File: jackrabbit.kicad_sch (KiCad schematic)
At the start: 62 parts, among them J1 USB_C, J2 PinHeader_2.54mm_02x10, J3 PinHeader_2.54mm_02x04, J4 PinHeader_2.54mm_02x04, J5 PinHeader_2.54mm_01x04, J6 PinHeader_2.54mm_01x03, SW1 SW_Push, SW2 SW_Push, U1 MIC5319-3.3YD5, U2 74LVX245, U3 W25Q16JVSNIQ, U4 RP2040, U5 74LVX245, Y1 ECS-120-18-33-JGN

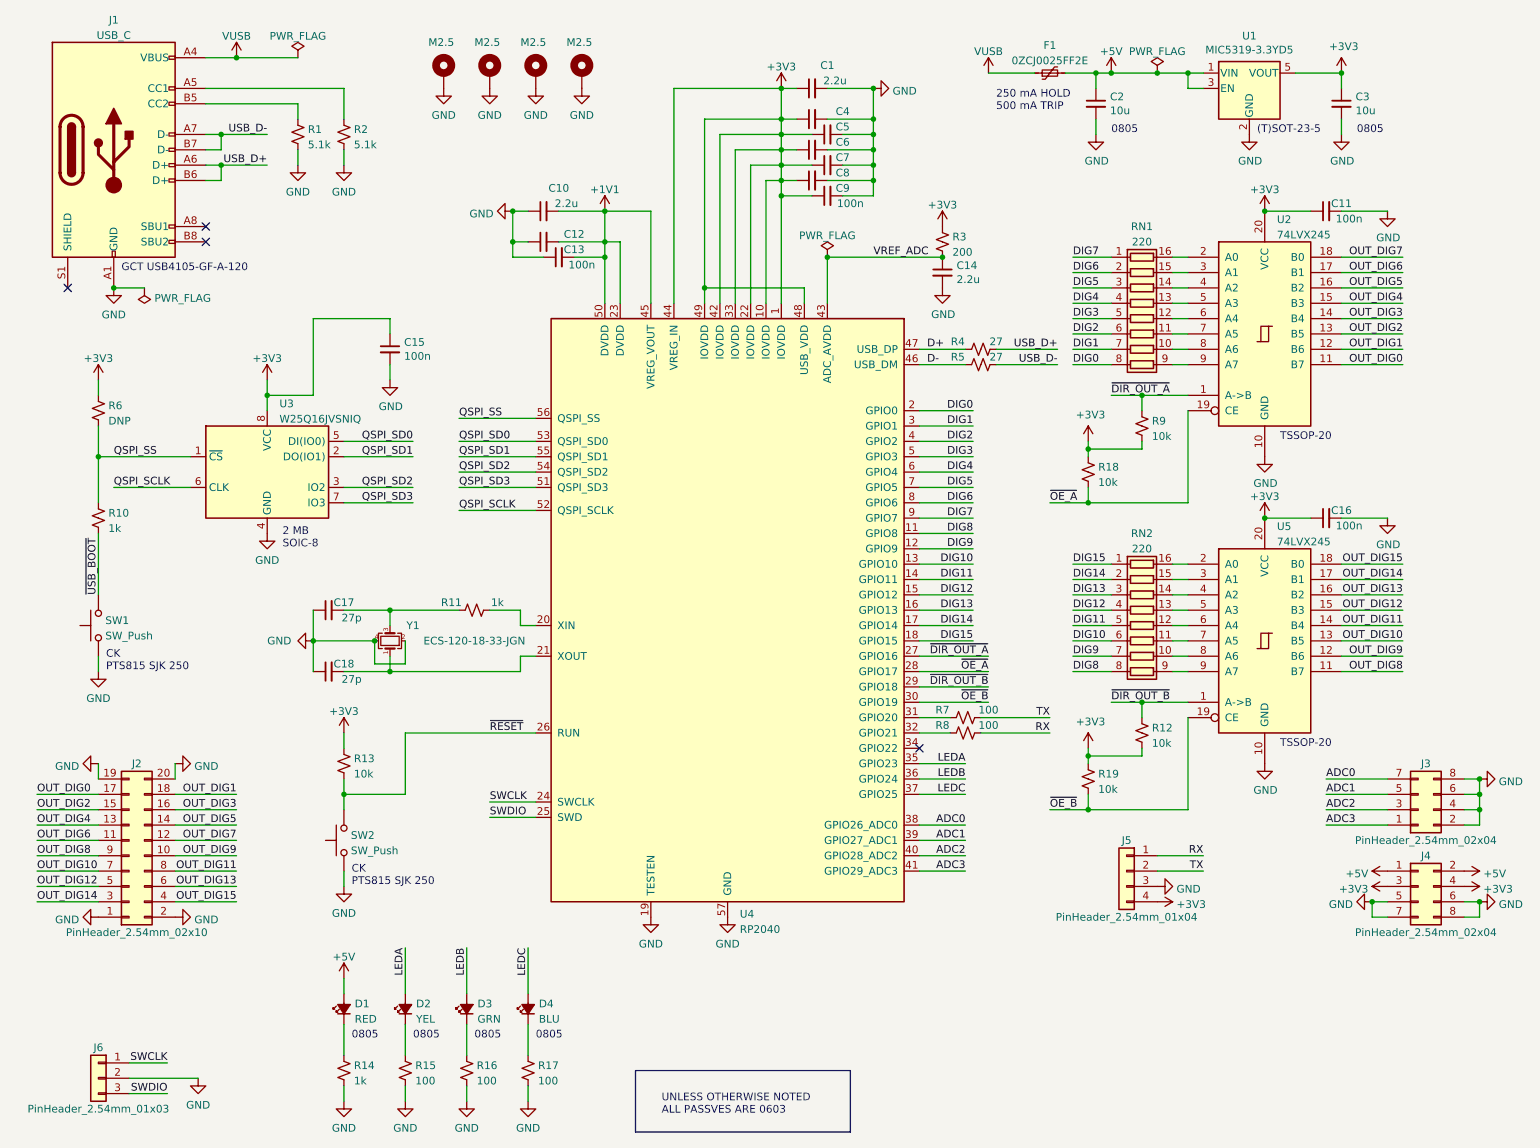
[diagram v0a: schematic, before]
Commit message: Connect bootsel button to a GPIO; remove connectors for which we have no room
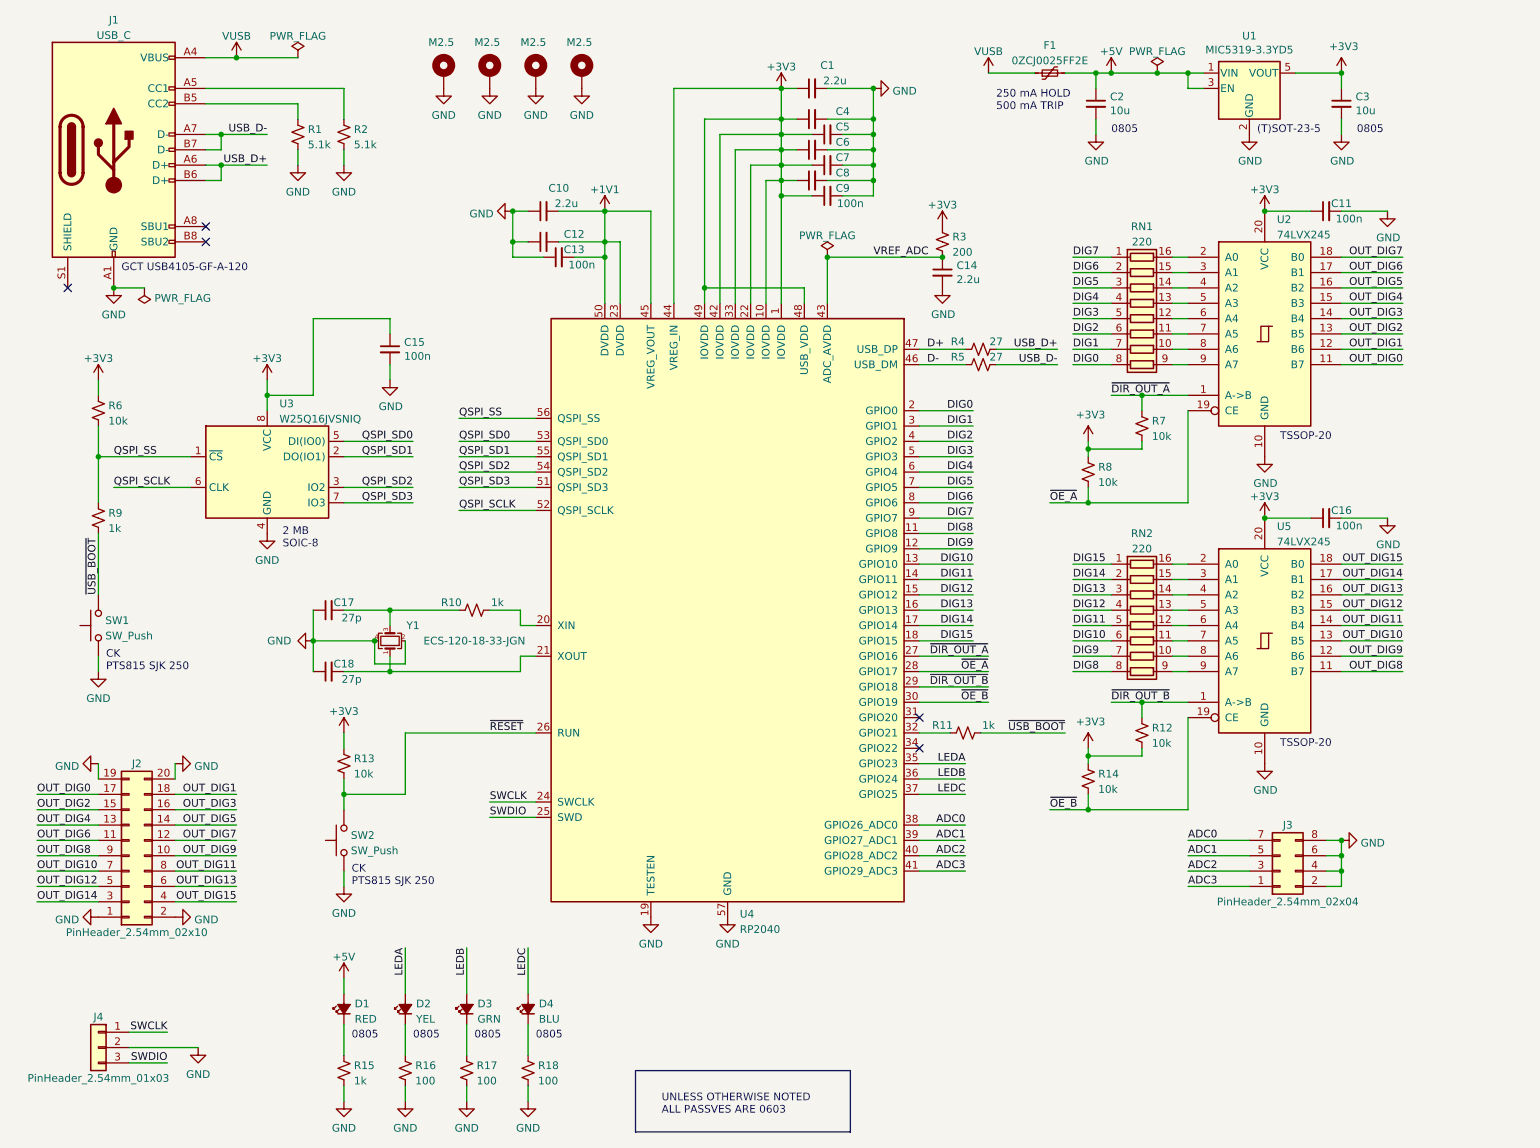
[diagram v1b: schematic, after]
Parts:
- removed J4: PinHeader_2.54mm_02x04, jackrabbit:PinHeader_2x04_P2.54mm_NoSilk, symbol Connector_Generic:Conn_02x04_Odd_Even
- removed J5: PinHeader_2.54mm_01x04, jackrabbit:PinHeader_1x04_P2.54mm_NoSilk, symbol Connector_Generic:Conn_01x04
- removed R8: 100, Resistor_SMD:R_0603_1608Metric_Pad0.98x0.95mm_HandSolder, symbol Device:R_Small_US
- R11: renamed from R7; value 100 -> 1k
- R6: value DNP -> 10k
- renumbered J6 to J4, R11 to R10, R19 to R14, R14 to R15, R15 to R16, R16 to R17, R17 to R18, R9 to R7, R18 to R8, R10 to R9
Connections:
- net TX is gone; now on net ~{USB_BOOT}: R11.2
- net at U4.31 (GPIO20): no longer R11.1
- net at U4.32 (GPIO21): now also R11.1
- no-connect marks 4 -> 5
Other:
- moved on the sheet: J3, J4, R11

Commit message: Flip LED labels to make 'A" the one by the USB connector
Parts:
- renumbered D4 to D2, D2 to D4
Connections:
- net LEDA: now also D2.2 (A), U4.37 (GPIO25); no longer D4.2 (A), U4.35 (GPIO23)
- net LEDC: now also D4.2 (A), U4.35 (GPIO23); no longer D2.2 (A), U4.37 (GPIO25)
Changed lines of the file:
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@@
     (effects (font (size 1.27 1.27)) (justify left bottom))
   )
-  (label "LEDC" (at 101.6 170.18 270)
+  (label "LEDA" (at 101.6 170.18 270)
     (effects (font (size 1.27 1.27)) (justify right bottom))
   )
@@
     (effects (font (size 1.27 1.27)) (justify right bottom))
   )
-  (label "LEDC" (at 173.99 144.78 180)
+  (label "LEDA" (at 173.99 144.78 180)
     (effects (font (size 1.27 1.27)) (justify right bottom))
   )
@@
     (effects (font (size 1.27 1.27)) (justify left bottom))
   )
-  (label "LEDA" (at 81.28 170.18 270)
+  (label "LEDC" (at 81.28 170.18 270)
     (effects (font (size 1.27 1.27)) (justify right bottom))
   )
@@
     (effects (font (size 1.27 1.27)) (justify right bottom))
   )
-  (label "LEDA" (at 173.99 139.7 180)
+  (label "LEDC" (at 173.99 139.7 180)
     (effects (font (size 1.27 1.27)) (justify right bottom))
   )
@@
   (symbol (lib_name "LED_Small_Filled_1") (lib_id "Device:LED_Small_Filled") (at 81.28 180.34 90) (unit 1)
     (in_bom yes) (on_board yes)
-    (property "Reference" "D2" (id 0) (at 83.058 179.4418 90)
+    (property "Reference" "D4" (id 0) (at 83.058 179.4418 90)
       (effects (font (size 1.27 1.27)) (justify right))
     )
@@
   (symbol (lib_name "LED_Small_Filled_1") (lib_id "Device:LED_Small_Filled") (at 101.6 180.34 90) (unit 1)
     (in_bom yes) (on_board yes)
-    (property "Reference" "D4" (id 0) (at 103.378 179.4418 90)
+    (property "Reference" "D2" (id 0) (at 103.378 179.4418 90)
       (effects (font (size 1.27 1.27)) (justify right))
     )
@@
       (reference "D1") (unit 1) (value "RED") (footprint "LED_SMD:LED_0805_2012Metric_Pad1.15x1.40mm_HandSolder")
     )
-    (path "/3c8ad82e-0820-4ead-9e14-c5a1d0d6fa95"
-      (reference "D2") (unit 1) (value "YEL") (footprint "LED_SMD:LED_0805_2012Metric_Pad1.15x1.40mm_HandSolder")
+    (path "/6e15d54a-aef5-43a5-a120-ced871729ae0"
+      (reference "D2") (unit 1) (value "BLU") (footprint "LED_SMD:LED_0805_2012Metric_Pad1.15x1.40mm_HandSolder")
     )
     (path "/0334377f-0ba8-4c56-8715-c44a67252a3c"
       (reference "D3") (unit 1) (value "GRN") (footprint "LED_SMD:LED_0805_2012Metric_Pad1.15x1.40mm_HandSolder")
     )
-    (path "/6e15d54a-aef5-43a5-a120-ced871729ae0"
-      (reference "D4") (unit 1) (value "BLU") (footprint "LED_SMD:LED_0805_2012Metric_Pad1.15x1.40mm_HandSolder")
+    (path "/3c8ad82e-0820-4ead-9e14-c5a1d0d6fa95"
+      (reference "D4") (unit 1) (value "YEL") (footprint "LED_SMD:LED_0805_2012Metric_Pad1.15x1.40mm_HandSolder")
     )
     (path "/0f88460d-2b2c-40e7-94ae-da4786e25a21"

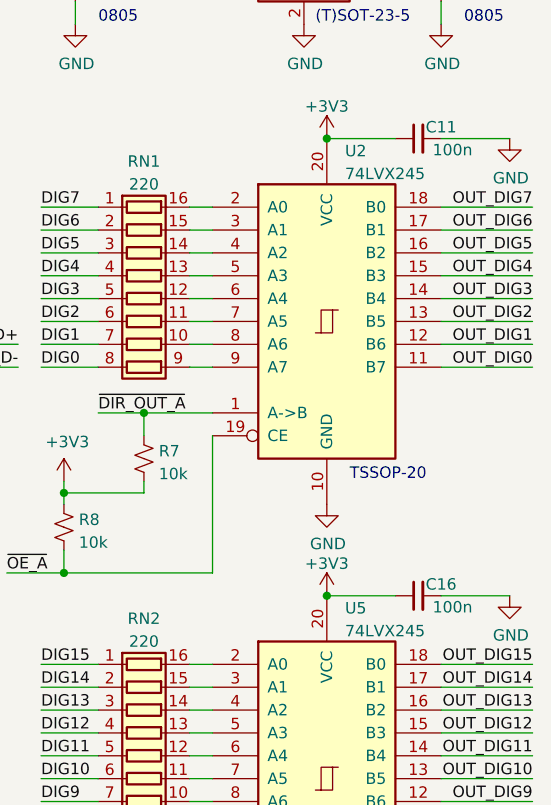
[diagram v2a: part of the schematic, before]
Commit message: Replace 74LCX245 with 74LVCH245A for bus hold to prevent floating input
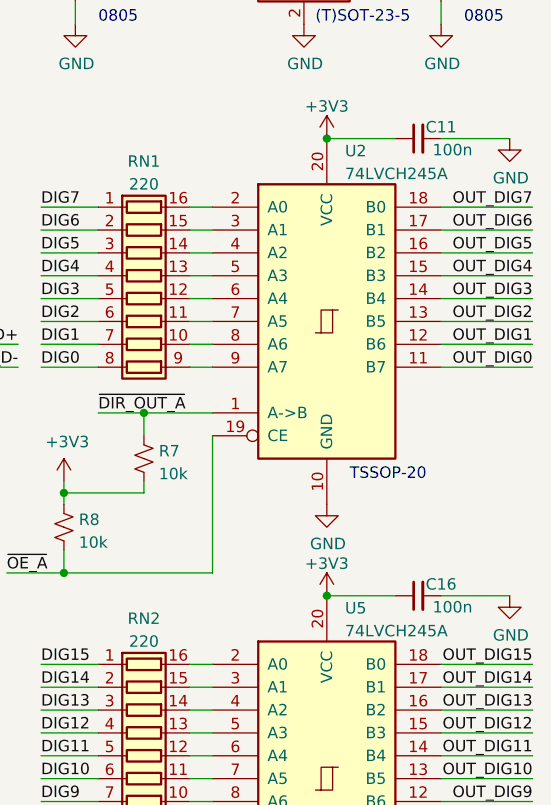
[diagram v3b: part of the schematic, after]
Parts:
- U2, U5: value 74LVX245 -> 74LVCH245A
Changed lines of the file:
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@@
       (effects (font (size 1.27 1.27)) (justify left))
     )
-    (property "Value" "74LVX245" (id 1) (at 225.5394 52.1771 0)
+    (property "Value" "74LVCH245A" (id 1) (at 225.5394 52.1771 0)
       (effects (font (size 1.27 1.27)) (justify left))
     )
@@
       (effects (font (size 1.27 1.27)) hide)
     )
-    (property "Datasheet" "https://www.mouser.com/datasheet/2/149/74LCX245-21038.pdf" (id 3) (at 223.52 68.58 0)
+    (property "Datasheet" "https://assets.nexperia.com/documents/data-sheet/74LVC_LVCH245A.pdf" (id 3) (at 223.52 68.58 0)
       (effects (font (size 1.27 1.27)) hide)
     )
@@
       (effects (font (size 1.27 1.27)) (justify left))
     )
-    (property "Value" "74LVX245" (id 1) (at 225.5394 102.9771 0)
+    (property "Value" "74LVCH245A" (id 1) (at 225.5394 102.9771 0)
       (effects (font (size 1.27 1.27)) (justify left))
     )
@@
       (effects (font (size 1.27 1.27)) hide)
     )
-    (property "Datasheet" "https://www.mouser.com/datasheet/2/149/74LCX245-21038.pdf" (id 3) (at 223.52 119.38 0)
+    (property "Datasheet" "https://assets.nexperia.com/documents/data-sheet/74LVC_LVCH245A.pdf" (id 3) (at 223.52 119.38 0)
       (effects (font (size 1.27 1.27)) hide)
     )
@@
     )
     (path "/0f4fbdea-f543-4ede-94c8-ede66639b964"
-      (reference "U2") (unit 1) (value "74LVX245") (footprint "Package_SO:TSSOP-20_4.4x5mm_P0.5mm")
+      (reference "U2") (unit 1) (value "74LVCH245A") (footprint "Package_SO:TSSOP-20_4.4x5mm_P0.5mm")
     )
     (path "/15efc400-9a3c-4e35-bd77-456d19e391d6"
@@
     )
     (path "/102b6500-7d2e-428a-b0d9-ecb98861e4f0"
-      (reference "U5") (unit 1) (value "74LVX245") (footprint "Package_SO:TSSOP-20_4.4x5mm_P0.5mm")
+      (reference "U5") (unit 1) (value "74LVCH245A") (footprint "Package_SO:TSSOP-20_4.4x5mm_P0.5mm")
     )
     (path "/bddb51ee-6644-4c08-a840-0f41d7938dbf"

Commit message: Make crystal footprint; check footprints
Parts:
- Y1: footprint Crystal:Crystal_SMD_SeikoEpson_FA238-4Pin_3.2x2.5mm -> jackrabbit:Crystal_SMD_ECS-4Pin_3.2x2.5mm
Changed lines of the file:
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@@
     (property "Reference" "Y1" (id 0) (at 82.55 116.84 90))
     (property "Value" "ECS-120-18-33-JGN" (id 1) (at 92.71 119.38 90))
-    (property "Footprint" "Crystal:Crystal_SMD_SeikoEpson_FA238-4Pin_3.2x2.5mm" (id 2) (at 78.74 119.38 0)
+    (property "Footprint" "jackrabbit:Crystal_SMD_ECS-4Pin_3.2x2.5mm" (id 2) (at 78.74 119.38 0)
       (effects (font (size 1.27 1.27)) hide)
     )
@@
     )
     (path "/bddb51ee-6644-4c08-a840-0f41d7938dbf"
-      (reference "Y1") (unit 1) (value "ECS-120-18-33-JGN") (footprint "Crystal:Crystal_SMD_SeikoEpson_FA238-4Pin_3.2x2.5mm")
-    )
-  )
+      (reference "Y1") (unit 1) (value "ECS-120-18-33-JGN") (footprint "jackrabbit:Crystal_SMD_ECS-4Pin_3.2x2.5mm")
+    )
+  )
